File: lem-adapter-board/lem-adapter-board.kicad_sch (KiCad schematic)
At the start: 13 parts, among them J7 Conn_01x04, J8 Conn_01x04, J9 Conn_02x10_Odd_Even

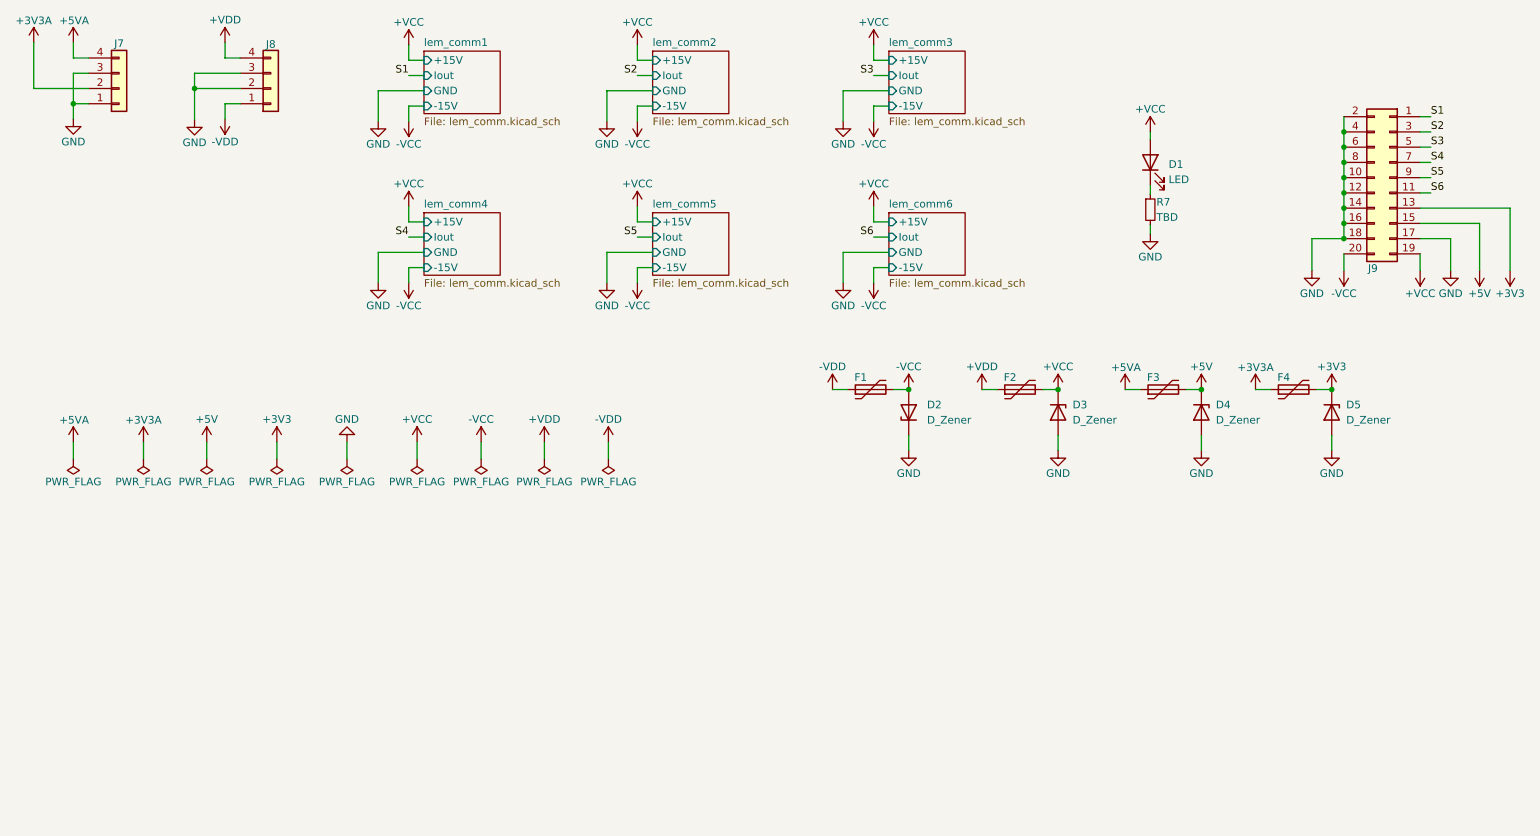
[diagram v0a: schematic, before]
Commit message: Changed order in lem adapter connector
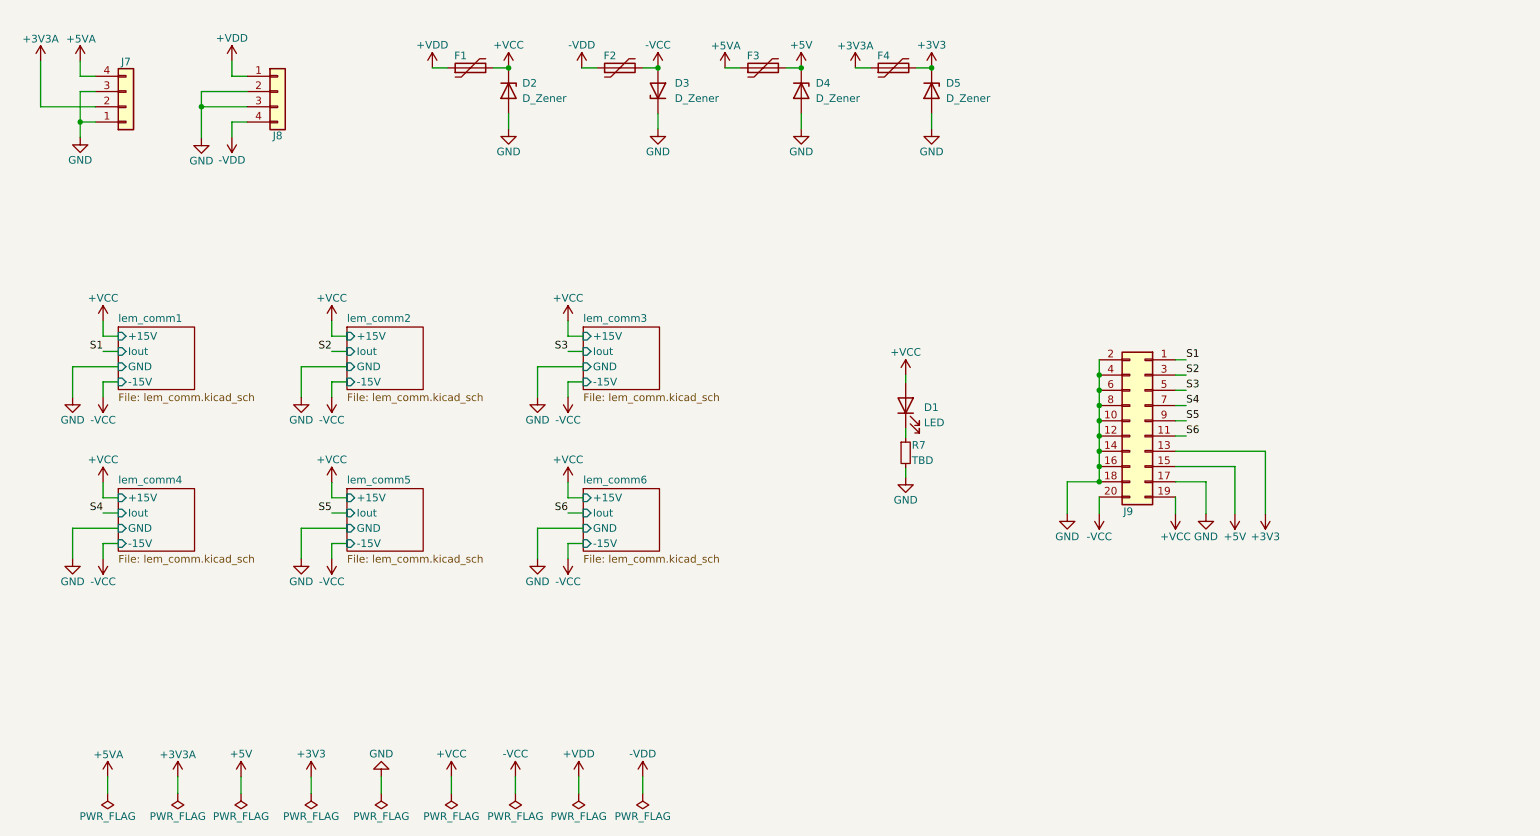
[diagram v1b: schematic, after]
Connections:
- net +VCC: now also D2.1 (K), F1.2; no longer D3.1 (K), F2.2
- net +VDD: now also F1.1, J8.1 (Pin_1); no longer F2.1, J8.4 (Pin_4)
- net -VCC: now also D3.2 (A), F2.2; no longer D2.2 (A), F1.2
- net -VDD: now also F2.1, J8.4 (Pin_4); no longer F1.1, J8.1 (Pin_1)
- net GND: now also D2.2 (A), D3.1 (K); no longer D2.1 (K), D3.2 (A)
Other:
- moved on the sheet: D1, D2, D3, D4, D5, F1, F2, F3, F4, J7, J8, J9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

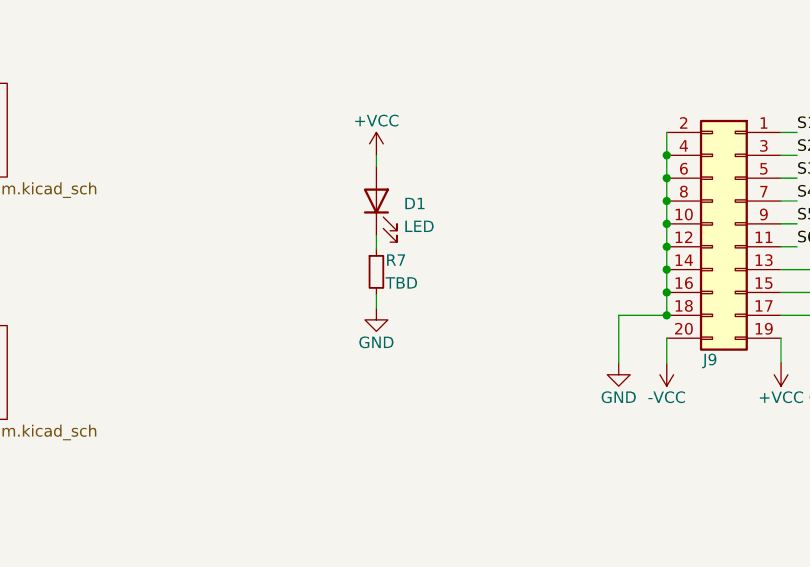
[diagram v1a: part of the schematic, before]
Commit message: Created bom for lem adapter board
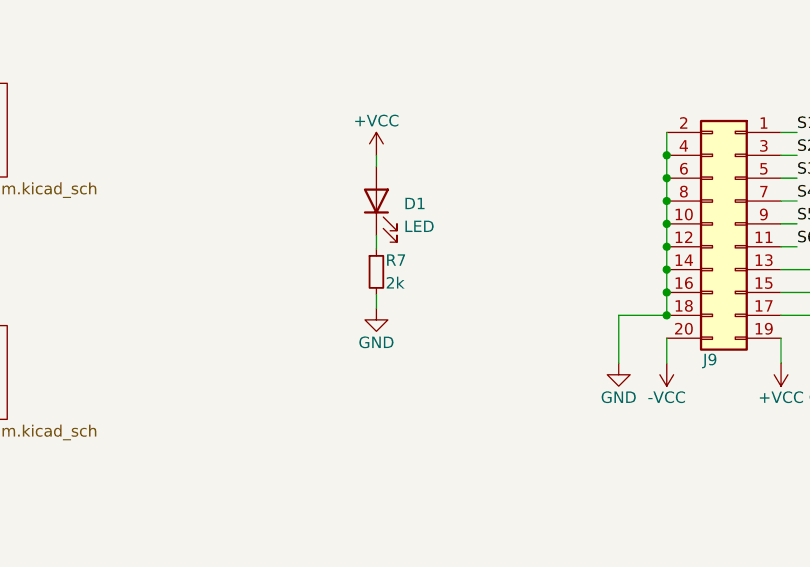
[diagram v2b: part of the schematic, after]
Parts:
- R7: value TBD -> 2k
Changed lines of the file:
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@@
       (effects (font (size 1.27 1.27)) (justify left))
     )
-    (property "Value" "TBD" (id 1) (at 165.1 88.392 0)
+    (property "Value" "2k" (id 1) (at 165.1 88.392 0)
       (effects (font (size 1.27 1.27)) (justify left))
     )
@@
     )
     (path "/ad4e0205-8d15-42a9-abfb-51f5bb30f379"
-      (reference "R7") (unit 1) (value "TBD") (footprint "Resistor_SMD:R_0805_2012Metric")
+      (reference "R7") (unit 1) (value "2k") (footprint "Resistor_SMD:R_0805_2012Metric")
     )
     (path "/b681418b-d66d-4947-8735-9d8a90ce1201/e9ad701c-262a-4a0a-8b6f-364c8702555b"
